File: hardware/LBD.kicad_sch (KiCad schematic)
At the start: 28 parts, among them J1 USB4155-03-C_REVA, SW1 SW_Push, U1 RP2040, U2 TPSM828214SILR, U3 W25Q128JVSIQ, Y1 Crystal_GND24

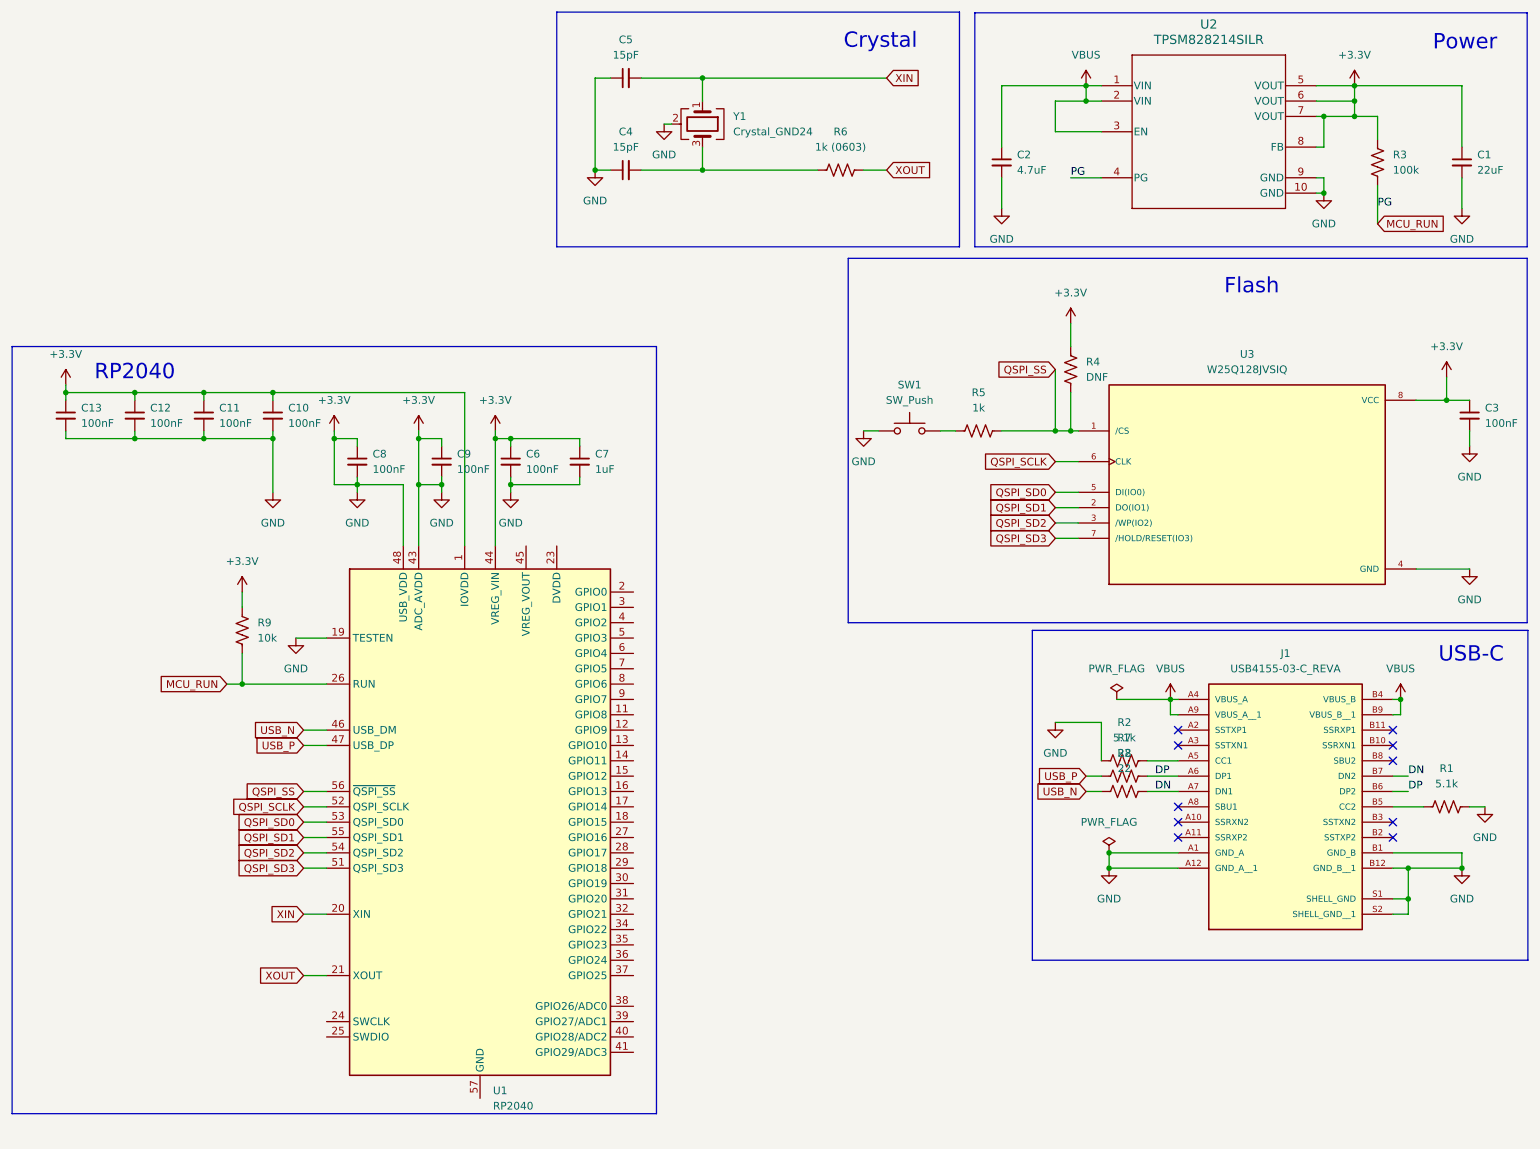
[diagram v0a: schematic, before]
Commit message: cleaned up schematic
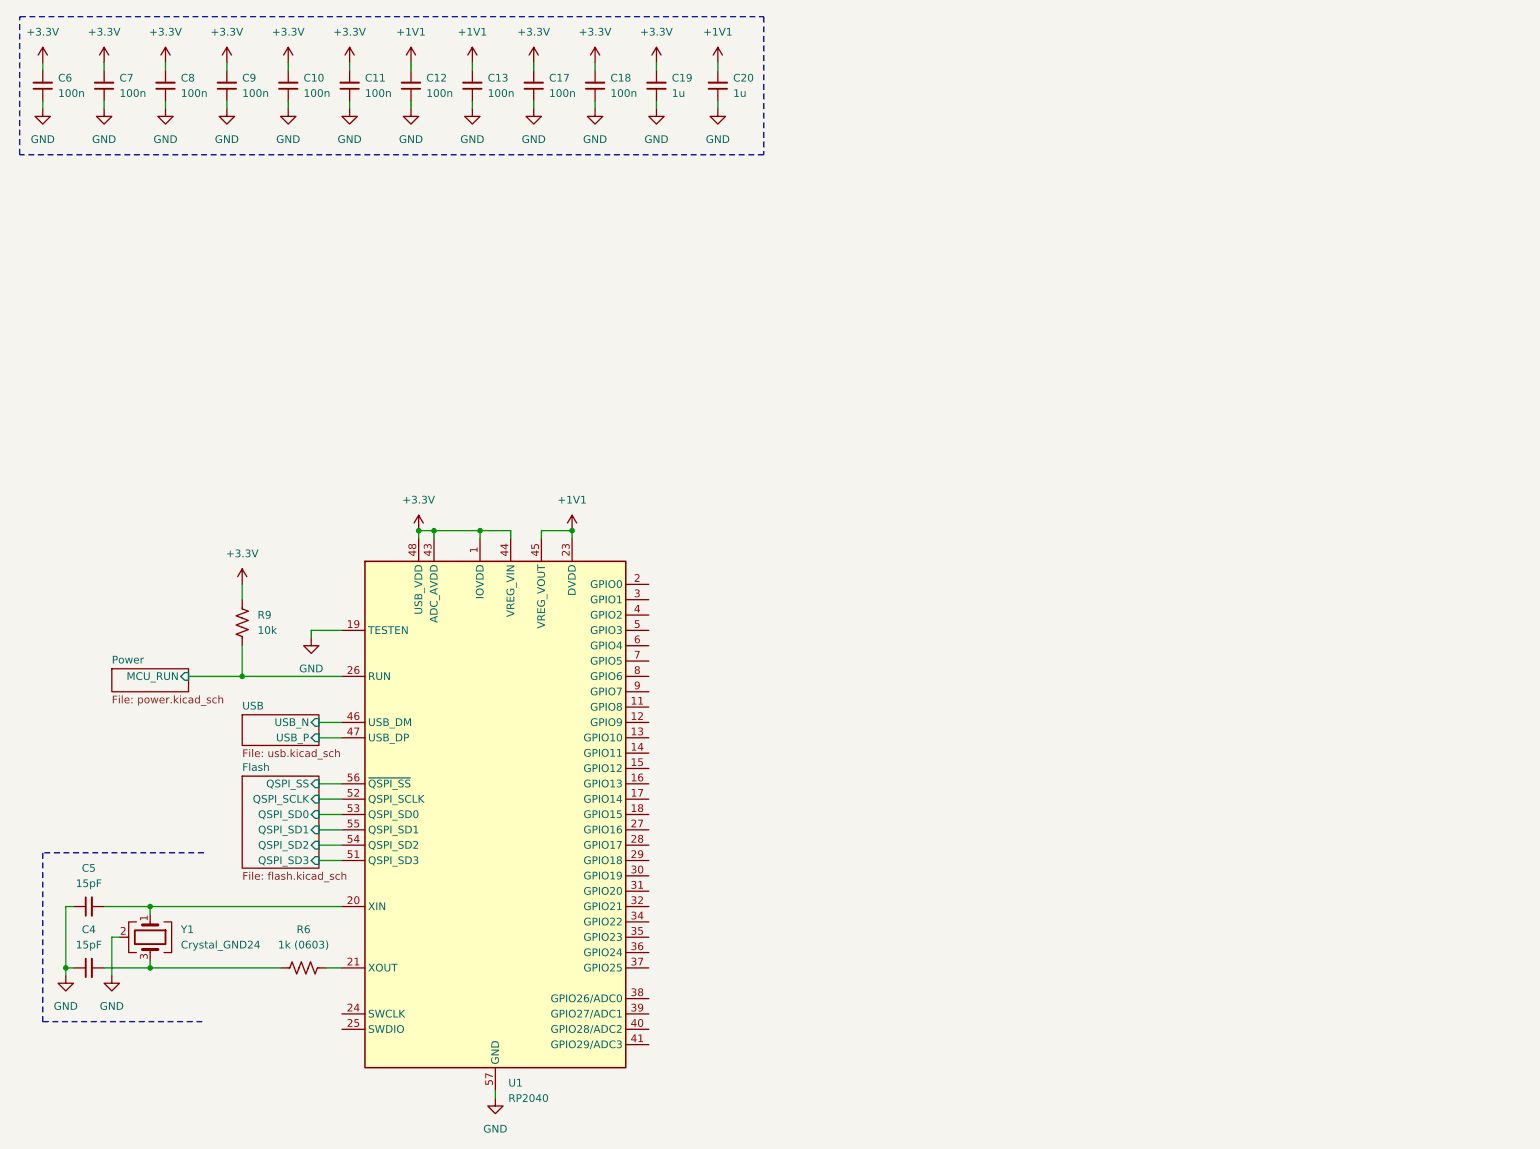
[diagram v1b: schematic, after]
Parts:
- removed C1: 22uF, symbol Device:C_Small
- removed C2: 4.7uF, symbol Device:C_Small
- removed C3: 100nF, symbol Device:C_Small
- removed J1: USB4155-03-C_REVA, USB4155-03-C_REVA:GCT_USB4155-03-C_REVA, symbol LBD_Library:USB4155-03-C_REVA
- removed R1, R2: 5.1k, symbol Device:R_US
- removed R3: 100k, symbol Device:R_US
- removed R4: DNF, symbol Device:R_US
- removed R5: 1k, symbol Device:R_US
- removed R7, R8: 22, symbol Device:R_US
- removed SW1: SW_Push, symbol Switch:SW_Push
- removed U2: TPSM828214SILR, SIL0010D-MFG, symbol LBD_Library:TPSM828214SILR
- removed U3: W25Q128JVSIQ, W25Q128JVSIQ:SOIC127P790X216-8N, symbol LBD_Library:W25Q128JVSIQ
- added C17, C18: 100n, symbol Device:C_Small
- added C19, C20: 1u, symbol Device:C_Small
- C10, C11, C12, C13, C6, C8, C9: value 100nF -> 100n
- C7: value 1uF -> 100n
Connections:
- net +3.3V: now also C17.2, C18.2, C19.2; no longer C10.1, C11.1, C12.1, C12.2, C13.1, C13.2, C4.1, C5.1, C6.1, C7.1, C8.1, C9.1, U1.19 (TESTEN), Y1.2 (G), Y1.4 (G)
- net +1V1: now reaches U1.23 (DVDD), U1.50 (DVDD)
- net +1V1: now also C12.2, C13.2, U1.45 (VREG_VOUT), C20.2
- net GND: now reaches U1.57 (GND)
- net GND: now also C10.1, C11.1, C12.1, C13.1, C4.1, C5.1, C6.1, C7.1, C8.1, C9.1, U1.19 (TESTEN), Y1.2 (G), Y1.4 (G), C17.1, C18.1, C19.1, C20.1
- net MCU_RUN renamed Power/MCU_RUN
- net QSPI_SCLK renamed Flash/QSPI_SCLK
- net QSPI_SD0 renamed Flash/QSPI_SD0
- net QSPI_SD1 renamed Flash/QSPI_SD1
- net QSPI_SD2 renamed Flash/QSPI_SD2
- net QSPI_SD3 renamed Flash/QSPI_SD3
- net QSPI_SS renamed Flash/QSPI_SS
- net USB_N renamed USB/USB_N
- net USB_P renamed USB/USB_P
- net XIN: no longer names the net of C5.2, U1.20 (XIN), Y1.1
- net XOUT: no longer names the net of R6.1, U1.21 (XOUT)
- no-connect marks 10 -> 0
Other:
- added sheet Flash (flash.kicad_sch)
- added sheet Power (power.kicad_sch)
- added sheet USB (usb.kicad_sch)
- note removed: "Crystal"
- note removed: "Flash"
- note removed: "Power"
- note removed: "RP2040"
- note removed: "USB-C"
- moved on the sheet: C4, C5, R6, R9, U1, Y1
